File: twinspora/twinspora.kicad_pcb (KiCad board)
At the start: 4 copper layers, 76.9 x 36.9 mm, 176 parts, among them J1 TYPE-C-31-M-12, J10 XY-SH1_0-4A61, J12 XY-SH1_0-5A61, J13 Conn_01x02, J14 Conn_01x03, J15 Conn_01x03, J2 XT30U-M, J3 XT60PW-M, J4 Conn_01x02, J5 XY-SH1_0-3A61, J6 XY-SH1_0-3A61, J7 Conn_01x02, J8 XY-SH1_0-6A51, J9 XY-SH1_0-6A51, Q1 AO3401A, SW2 TS1187A26020, SW3 TS1187A26020, U1 STM32G473RBTx, U10 SRV05-4A, U11 SRV05-4A, U12 SRV05-4A, U2 SRV05-4A, U3 SRV05-4A, U4 XC6206P332MR, U5 CA-IF1044VD-Q1, U6 DRV8316CRRGFR, U7 DRV8316CRRGFR, U8 MT6701QT, U9 MT6701QT, X1 X322512MSB4SI

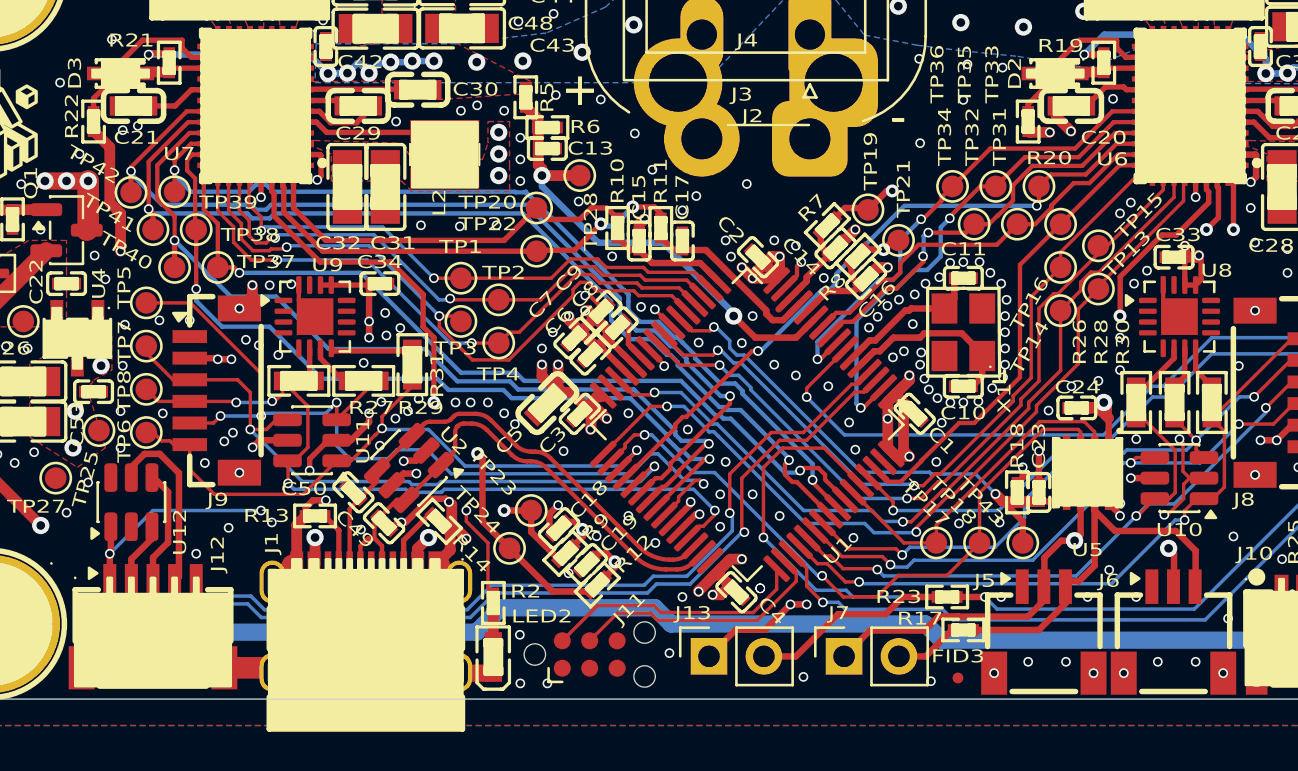
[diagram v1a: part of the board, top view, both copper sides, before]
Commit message: CAN wrong pinout
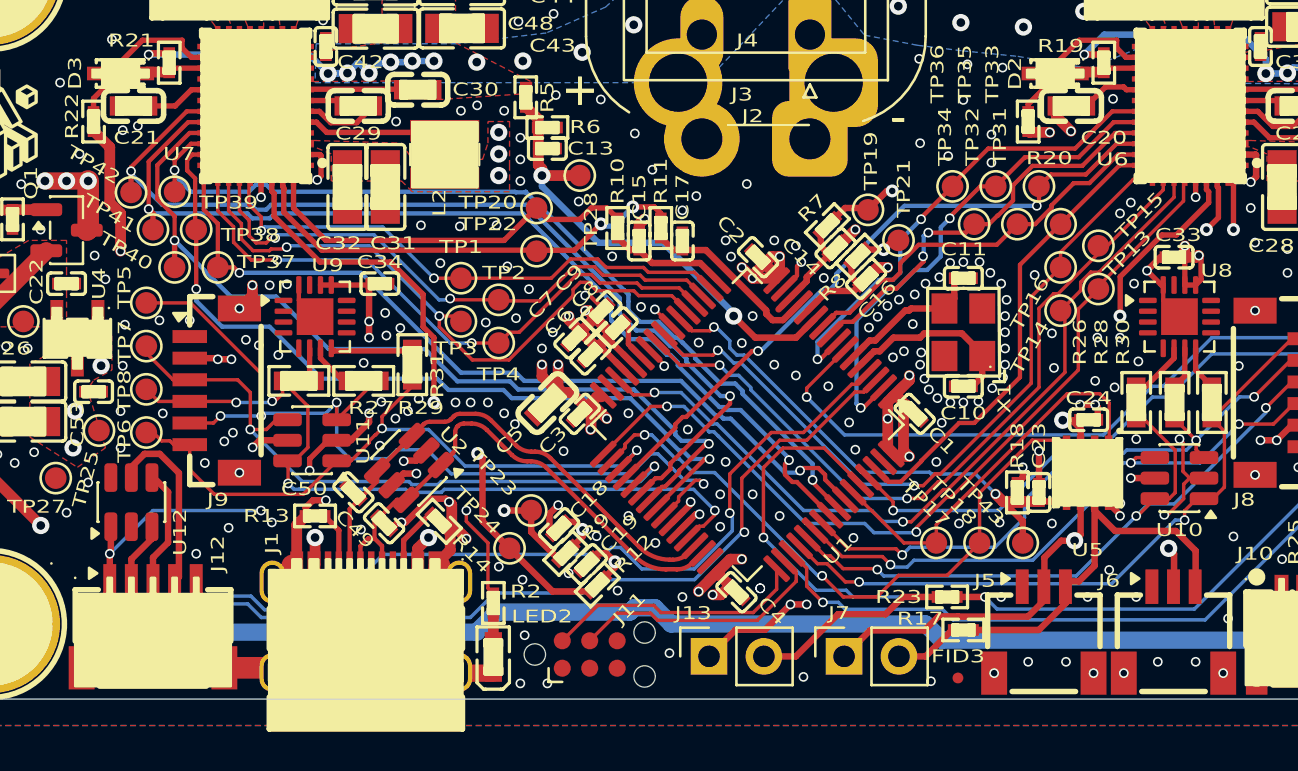
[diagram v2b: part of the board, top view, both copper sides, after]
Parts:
- moved C24 0.78 mm to (130.8, 124.8), turned to 180 degrees
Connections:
- U5 pad 1: +5V -> /FDCAN_TX
- U5 pad 2: /FDCAN_TX -> GND
- U5 pad 3: /FDCAN_RX -> +5V
- U5 pad 4: GND -> /FDCAN_RX
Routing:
- net +5V: track 98.2 -> 94.8 mm
- net /FDCAN_TX: track 15.6 -> 18.2 mm
- net GND: track 61.5 -> 63.0 mm, vias 310 -> 327
- net /FDCAN_RX: track 30.5 -> 29.2 mm
- net /GPIO2: track 45.4 -> 46.3 mm

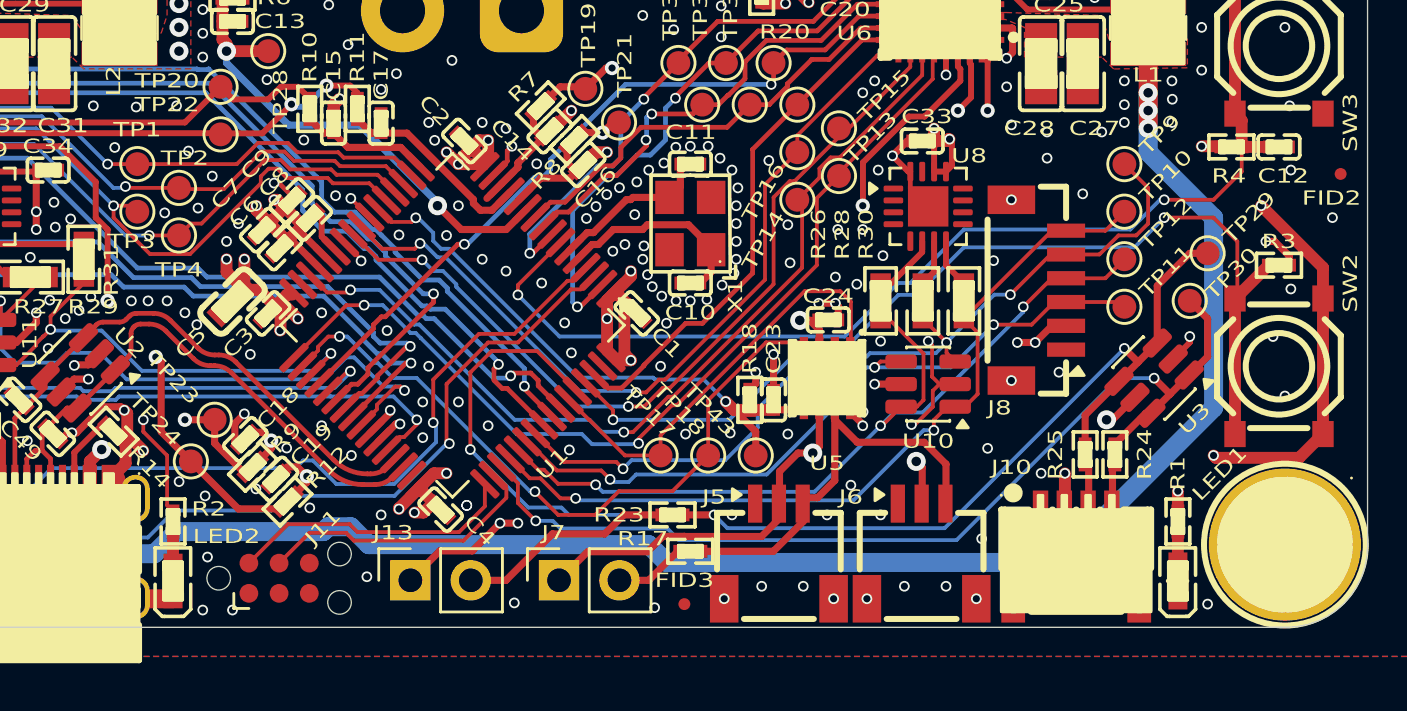
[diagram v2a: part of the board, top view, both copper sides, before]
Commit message: more stitching vias
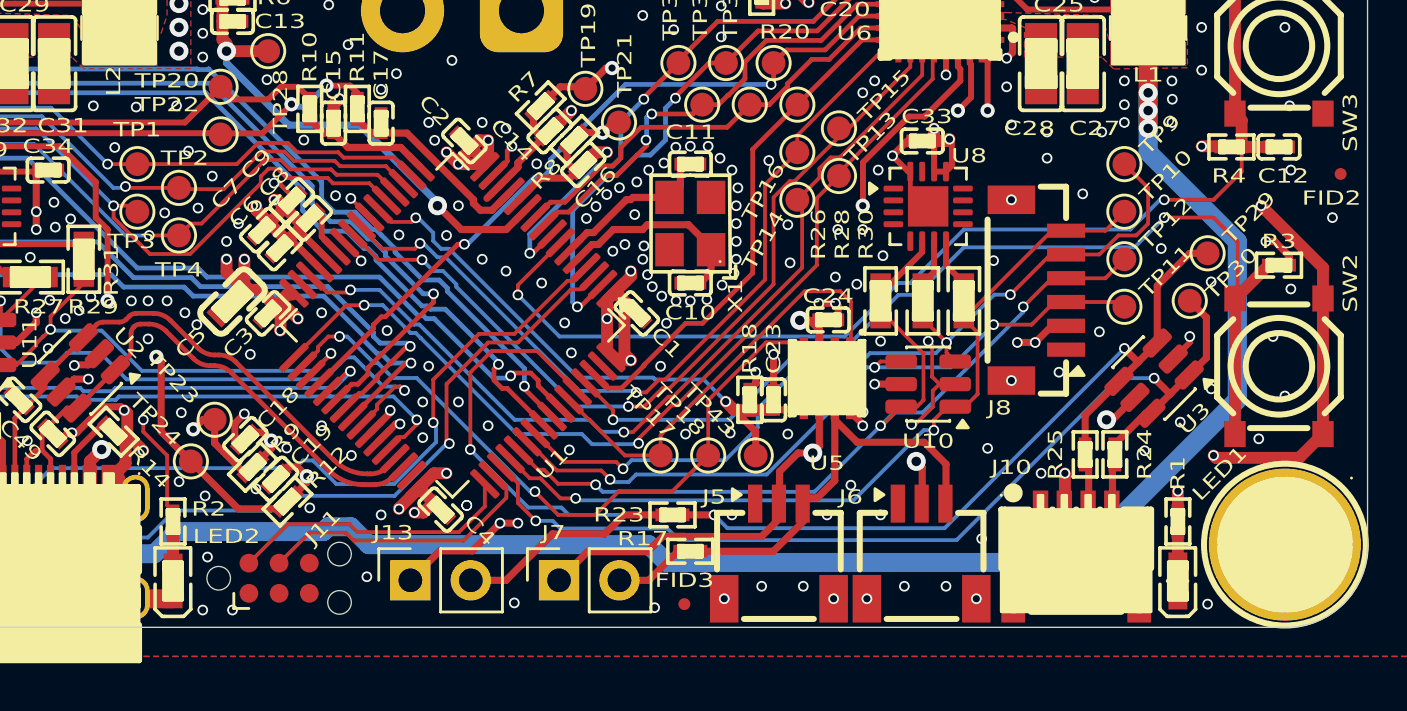
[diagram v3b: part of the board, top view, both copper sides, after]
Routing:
- net /5V_BKOUT: track 90.8 -> 91.6 mm
- net /SOC1: track 47.3 -> 46.6 mm
- net GND: vias 327 -> 337

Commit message: NEW
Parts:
- removed SW3: TS1187A26020, Switch:SW-SMD_4P-L5.2-W5.2-1
- added C54: EEEFT1H331GP, Capacitor_SMD_UWRL:CAP-SMD_BD10.0-L10.3-W10.3-LS11.0-R-RD, F.Cu at (89.1, 84.0)
- added C55: EEEFT1H331GP, Capacitor_SMD_UWRL:CAP-SMD_BD10.0-L10.3-W10.3-LS11.0-R-RD, F.Cu at (89.1, 70.4)
- added D4: 1N4148WS, Diode_SMD:D_SOD-323, F.Cu at (100.5, 86.5)
- added SW1: SKSGPAE010, Switch_UWRL:SW-SMD_SKSGAAE010, F.Cu at (64.4, 107.6)
- added U13: WSD4066DN, Transistor_FET_UWRL:DFN-8_L3.2-W3.1-P0.65-LS3.4-BL-EP, F.Cu at (69.0, 107.9)
- added U14: FMMT620TA, Transistor_BJT_UWRL:SOT-23-3_L2.9-W1.6-P1.90-LS2.8-BR, F.Cu at (69.0, 112.6)
- added U15: BK22C07-4DP/2-0_4V(800), Connector_HRS_BK22:CONN-SMD_4P-P0.40_BAM04-08073-0414, F.Cu at (101.2, 79.9)
- added U16: BK22C07-4DP/2-0_4V(800), Connector_HRS_BK22:CONN-SMD_4P-P0.40_BAM04-08073-0414, F.Cu at (101.2, 83.3)
- C1, C10, C11, C12, C13, C14, C15, C16, C17, C18, C19, C2, C22, C23, C24, C3, C35, C4, C42, C49, C50, C53, C6, C7, C8, C9: footprint Basic_Capacitors_Resistors:C0402 -> Capacitor_SMD:C_0402_1005Metric
- C27, C28, C31, C32, C36, C37, C38, C39, C40, C41, C43, C44, C45, C46, C47, C48, C51, C52: footprint Basic_Capacitors_Resistors:C0805 -> Capacitor_SMD:C_0805_2012Metric
- C5: footprint Basic_Capacitors_Resistors:C0603 -> Capacitor_SMD:C_0603_1608Metric
- D2, D3: value BZT52B5V1S -> BZT52B5V1S_C19077434; footprint Diode:SOD-323_L1.7-W1.3-LS2.6-RD -> Diode_SMD:D_SOD-323_HandSoldering
- R1, R10, R11, R12, R13, R14, R15, R16, R17, R18, R19, R2, R20, R21, R22, R23, R24, R25, R3, R4, R5, R6, R7, R8, R9: footprint Basic_Capacitors_Resistors:R0402 -> Resistor_SMD:R_0402_1005Metric
- SW2: value TS1187A26020 -> SKSGPAE010; footprint Switch:SW-SMD_4P-L5.2-W5.2-1 -> Switch_UWRL:SW-SMD_SKSGAAE010
- moved SW2 86.7 mm to (64.4, 111.5), turned to 0 degrees
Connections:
- C20 pad 2: Net-(U6-AVDD) -> Net-(U6-DRVOFF)
- C21 pad 2: Net-(U7-AVDD) -> Net-(U7-DRVOFF)
- C25 pad 1: Net-(U6-CPL) -> unconnected-(C25-Pad1)
- C25 pad 2: Net-(U6-CPH) -> unconnected-(C25-Pad2)
- C26 pad 2: Net-(U6-CP) -> unconnected-(C26-Pad2)
- C29 pad 1: Net-(U7-CPL) -> unconnected-(C29-Pad1)
- C29 pad 2: Net-(U7-CPH) -> unconnected-(C29-Pad2)
- C30 pad 2: Net-(U7-CP) -> unconnected-(C30-Pad2)
- L1 pad 2: Net-(U6-SW_BK) -> Net-(L1-Pad2)
- L2 pad 2: Net-(U7-SW_BK) -> Net-(L2-Pad2)
- R20 pad 2: Net-(U6-nFAULT) -> Net-(U6-nSLEEP)
- R22 pad 2: Net-(U7-nFAULT) -> Net-(U7-nSLEEP)
- SW2 pad 2: +3.3V -> /BOOT
- SW2 pad 3: /BOOT -> +3.3V
- U6 pad 13: /PHA1 -> /5V_BKOUT
- U6 pad 14: /PHA1 -> unconnected-(U6-OUTA-Pad14)
- U6 pad 16: /PHB1 -> unconnected-(U6-OUTB-Pad16)
- U6 pad 17: /PHB1 -> unconnected-(U6-OUTB-Pad17)
- U6 pad 19: /PHC1 -> Net-(L1-Pad2)
- U6 pad 20: /PHC1 -> GND
- U6 pad 21: unconnected-(U6-DRVOFF-Pad21) -> Net-(U6-DRVOFF)
- U6 pad 22: Net-(U6-nFAULT) -> Net-(D2-K)
- U6 pad 23: Net-(D2-K) -> Net-(U6-nSLEEP)
- U6 pad 25: Net-(U6-AVDD) -> unconnected-(U6-AVDD-Pad25)
- U6 pad 3: /5V_BKOUT -> /PHA1
- U6 pad 37: +3.3V -> unconnected-(U6-VREF/ILIM-Pad37)
- U6 pad 4: GND -> /PHA1
- U6 pad 5: Net-(U6-SW_BK) -> /PHB1
- U6 pad 6: Net-(U6-CPL) -> /PHB1
- U6 pad 7: Net-(U6-CPH) -> /PHC1
- U6 pad 8: Net-(U6-CP) -> /PHC1
- U7 pad 13: /PHA2 -> /BUCK
- U7 pad 14: /PHA2 -> unconnected-(U7-OUTA-Pad14)
- U7 pad 16: /PHB2 -> unconnected-(U7-OUTB-Pad16)
- U7 pad 17: /PHB2 -> unconnected-(U7-OUTB-Pad17)
- U7 pad 19: /PHC2 -> Net-(L2-Pad2)
- U7 pad 20: /PHC2 -> GND
- U7 pad 21: unconnected-(U7-DRVOFF-Pad21) -> Net-(U7-DRVOFF)
- U7 pad 22: Net-(U7-nFAULT) -> Net-(D3-K)
- U7 pad 23: Net-(D3-K) -> Net-(U7-nSLEEP)
- U7 pad 25: Net-(U7-AVDD) -> unconnected-(U7-AVDD-Pad25)
- U7 pad 3: /BUCK -> /PHA2
- U7 pad 37: +3.3V -> unconnected-(U7-VREF/ILIM-Pad37)
- U7 pad 4: GND -> /PHA2
- U7 pad 5: Net-(U7-SW_BK) -> /PHB2
- U7 pad 6: Net-(U7-CPL) -> /PHB2
- U7 pad 7: Net-(U7-CPH) -> /PHC2
- U7 pad 8: Net-(U7-CP) -> /PHC2
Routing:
- net (no net): track 2.02 -> 23.1 mm
- net /PHB1: track 0.00 -> 10.8 mm
- net /PHB2: track 0.00 -> 10.2 mm
- net Net-(U7-nFAULT): track 7.83 -> 0.00 mm
- net Net-(U6-nFAULT): track 7.58 -> 0.00 mm
- net Net-(U6-SW_BK): track 6.78 -> 0.00 mm
- net Net-(U7-SW_BK): track 6.58 -> 0.00 mm
- net /PHC1: track 0.00 -> 6.42 mm
- net /PHC2: track 0.00 -> 6.17 mm
- net Net-(U7-CP): track 4.42 -> 0.00 mm
- net Net-(U6-CP): track 4.42 -> 0.00 mm
- net Net-(U6-CPL): track 3.98 -> 0.00 mm
- net Net-(U7-CPL): track 3.59 -> 0.00 mm
- net Net-(U7-AVDD): track 2.86 -> 0.00 mm
- net Net-(U6-AVDD): track 2.82 -> 0.00 mm
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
